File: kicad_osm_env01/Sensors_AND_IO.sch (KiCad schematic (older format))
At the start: 52 parts, among them J4 Conn_01x08, J8 STX-3000, Q5 FK3503010L, Q6 SSM3J328R, U10 ICS-43434, U11 HDC2080, U12 TSL2561, U9 M74VHC1GT14DFT2G

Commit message: updated schematics
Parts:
- removed C44: 100nF, Capacitor_SMD:C_0402_1005Metric, symbol OSM_env01-rescue:C-device-ESP32-EVB_Rev_D-rescue
- removed R102: DNF, Resistor_SMD:R_0603_1608Metric, symbol OSM_env01-rescue:R-device-ESP32-EVB_Rev_D-rescue
- removed R103: 0R, Resistor_SMD:R_0603_1608Metric, symbol OSM_env01-rescue:R-device-ESP32-EVB_Rev_D-rescue
- removed TP49, TP82: Test_Point, TestPoint:TestPoint_THTPad_D1.0mm_Drill0.5mm, symbol OSM_env01-rescue:Test_Point-Connector-ESP32-EVB_Rev_D-rescue
- removed U12: TSL2561, Devtank_PCB_lib:TSL2561T_ALS, symbol OSM_env01-rescue:TSL2561-Devtank-ESP32-EVB_Rev_D-rescue
- added U3: VEML7700-TT, Devtank_PCB_lib:VEML7700-TT, symbol Devtank:VEML7700-TT
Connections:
- wire segments 141 -> 126
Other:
- note removed: "Light Sensor\n"
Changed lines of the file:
@@
 Wire Wire Line
 	3450 1075 3450 1150
-Text Notes 8900 4150 0    118  ~ 0
-Light Sensor\n
 $Sheet
 S 8600 4875 900  1000
@@
 Wire Wire Line
 	10100 5350 10050 5350
-$Comp
-L OSM_env01-rescue:R-device-ESP32-EVB_Rev_D-rescue R?
-U 1 1 6095989E
-P 7975 3125
-AR Path="/6095989E" Ref="R?"  Part="1"
-AR Path="/608F4675/6095989E" Ref="R102"  Part="1"
-F 0 "R102" H 8045 3171 50  0000 L CNN
-F 1 "DNF" H 8045 3080 50  0000 L CNN
-F 2 "Resistor_SMD:R_0603_1608Metric" V 7905 3125 50  0001 C CNN
-F 3 "" H 7975 3125 50  0001 C CNN
-	1    7975 3125
-	1    0    0    -1
-$EndComp
-$Comp
-L OSM_env01-rescue:R-device-ESP32-EVB_Rev_D-rescue R?
-U 1 1 609598A4
-P 7975 3500
-AR Path="/609598A4" Ref="R?"  Part="1"
-AR Path="/608F4675/609598A4" Ref="R103"  Part="1"
-F 0 "R103" H 8045 3546 50  0000 L CNN
-F 1 "0R" H 8045 3455 50  0000 L CNN
-F 2 "Resistor_SMD:R_0603_1608Metric" V 7905 3500 50  0001 C CNN
-F 3 "" H 7975 3500 50  0001 C CNN
-	1    7975 3500
-	1    0    0    -1
-$EndComp
-Wire Wire Line
-	7975 3300 7975 3275
-Wire Wire Line
-	7975 3350 7975 3300
-Connection ~ 7975 3300
-$Comp
-L power:+3V3 #PWR?
-U 1 1 609598AD
-P 8775 2775
-AR Path="/609598AD" Ref="#PWR?"  Part="1"
-AR Path="/608F4675/609598AD" Ref="#PWR089"  Part="1"
-F 0 "#PWR089" H 8775 2625 50  0001 C CNN
-F 1 "+3V3" H 8790 2948 50  0000 C CNN
-F 2 "" H 8775 2775 50  0001 C CNN
-F 3 "" H 8775 2775 50  0001 C CNN
-	1    8775 2775
-	1    0    0    -1
-$EndComp
-$Comp
-L power:+3V3 #PWR?
-U 1 1 609598B3
-P 7975 2950
-AR Path="/609598B3" Ref="#PWR?"  Part="1"
-AR Path="/608F4675/609598B3" Ref="#PWR085"  Part="1"
-F 0 "#PWR085" H 7975 2800 50  0001 C CNN
-F 1 "+3V3" H 7990 3123 50  0000 C CNN
-F 2 "" H 7975 2950 50  0001 C CNN
-F 3 "" H 7975 2950 50  0001 C CNN
-	1    7975 2950
-	1    0    0    -1
-$EndComp
-Wire Wire Line
-	7975 2975 7975 2950
-$Comp
-L OSM_env01-rescue:GND-ESP32-EVB_Rev_D #PWR?
-U 1 1 609598BA
-P 7975 3725
-AR Path="/609598BA" Ref="#PWR?"  Part="1"
-AR Path="/608F4675/609598BA" Ref="#PWR086"  Part="1"
-F 0 "#PWR086" H 7975 3475 50  0001 C CNN
-F 1 "GND" H 7980 3552 50  0000 C CNN
-F 2 "" H 7975 3725 60  0000 C CNN
-F 3 "" H 7975 3725 60  0000 C CNN
-	1    7975 3725
-	1    0    0    -1
-$EndComp
-$Comp
-L OSM_env01-rescue:GND-ESP32-EVB_Rev_D #PWR?
-U 1 1 609598C0
-P 8900 3725
-AR Path="/609598C0" Ref="#PWR?"  Part="1"
-AR Path="/608F4675/609598C0" Ref="#PWR090"  Part="1"
-F 0 "#PWR090" H 8900 3475 50  0001 C CNN
-F 1 "GND" H 8905 3552 50  0000 C CNN
-F 2 "" H 8900 3725 60  0000 C CNN
-F 3 "" H 8900 3725 60  0000 C CNN
-	1    8900 3725
-	1    0    0    -1
-$EndComp
-Wire Wire Line
-	8900 3725 8900 3475
-Wire Wire Line
-	8900 3475 8975 3475
-Wire Wire Line
-	7975 3725 7975 3650
-$Comp
-L OSM_env01-rescue:C-device-ESP32-EVB_Rev_D-rescue C?
-U 1 1 609598CB
-P 8625 2975
-AR Path="/609598CB" Ref="C?"  Part="1"
-AR Path="/608F4675/609598CB" Ref="C44"  Part="1"
-F 0 "C44" H 8750 3075 50  0000 L CNN
-F 1 "100nF" H 8750 3000 50  0000 L CNN
-F 2 "Capacitor_SMD:C_0402_1005Metric" H 8663 2825 50  0001 C CNN
-F 3 "" H 8625 2975 50  0001 C CNN
-	1    8625 2975
-	0    -1   -1   0
-$EndComp
-Wire Wire Line
-	8975 3125 8775 3125
-$Comp
-L OSM_env01-rescue:TSL2561-Devtank-ESP32-EVB_Rev_D-rescue U?
-U 1 1 609598E0
-P 9475 3300
-AR Path="/609598E0" Ref="U?"  Part="1"
-AR Path="/608F4675/609598E0" Ref="U12"  Part="1"
-F 0 "U12" H 9487 3740 50  0000 C CNN
-F 1 "TSL2561" H 9487 3649 50  0000 C CNN
-F 2 "Devtank_PCB_lib:TSL2561T_ALS" H 9500 2950 50  0001 C CNN
-F 3 "http://www.ti.com/lit/ds/symlink/hdc1080.pdf" H 9275 3625 50  0001 C CNN
-	1    9475 3300
-	1    0    0    -1
-$EndComp
-Wire Wire Line
-	10000 3125 10550 3125
-Wire Wire Line
-	10000 3600 10575 3600
-Wire Wire Line
-	8775 2775 8775 2975
-Connection ~ 8775 2975
-Wire Wire Line
-	8775 2975 8775 3125
-$Comp
-L OSM_env01-rescue:GND-ESP32-EVB_Rev_D #PWR?
-U 1 1 609598EB
-P 8375 2975
-AR Path="/609598EB" Ref="#PWR?"  Part="1"
-AR Path="/608F4675/609598EB" Ref="#PWR088"  Part="1"
-F 0 "#PWR088" H 8375 2725 50  0001 C CNN
-F 1 "GND" H 8380 2802 50  0000 C CNN
-F 2 "" H 8375 2975 60  0000 C CNN
-F 3 "" H 8375 2975 60  0000 C CNN
-	1    8375 2975
-	1    0    0    -1
-$EndComp
-Wire Wire Line
-	8375 2975 8475 2975
-Wire Wire Line
-	7975 3300 8975 3300
 Text Notes 8125 6300 0    118  ~ 0
 Sound Level Meter\n
@@
 Text HLabel 7650 1025 0    50   Input ~ 0
 SDA
-Text HLabel 10550 3125 2    50   Input ~ 0
-SDA
-Text HLabel 10575 3600 2    50   Input ~ 0
-SCL
-Wire Wire Line
-	10000 3600 10000 3475
 Wire Wire Line
 	10200 5450 10050 5450
@@
 Text HLabel 8275 5350 0    50   Input ~ 0
 MIC_GND
-Wire Wire Line
-	10000 3300 10400 3300
 Wire Wire Line
 	8250 5475 8375 5475
@@
 $Comp
 L OSM_env01-rescue:Test_Point-Connector-ESP32-EVB_Rev_D-rescue TP?
-U 1 1 60A1D280
-P 10400 3300
-AR Path="/5F6F7717/60A1D280" Ref="TP?"  Part="1"
-AR Path="/60A1D280" Ref="TP?"  Part="1"
-AR Path="/608F4675/60A1D280" Ref="TP82"  Part="1"
-F 0 "TP82" V 10400 3575 50  0000 C CNN
-F 1 "Test_Point" V 10475 3525 50  0001 C CNN
-F 2 "TestPoint:TestPoint_THTPad_D1.0mm_Drill0.5mm" H 10600 3300 50  0001 C CNN
-F 3 "~" H 10600 3300 50  0001 C CNN
-	1    10400 3300
-	0    1    1    0
-$EndComp
-$Comp
-L OSM_env01-rescue:Test_Point-Connector-ESP32-EVB_Rev_D-rescue TP?
-U 1 1 60A24650
-P 7975 3300
-AR Path="/5F6F7717/60A24650" Ref="TP?"  Part="1"
-AR Path="/60A24650" Ref="TP?"  Part="1"
-AR Path="/608F4675/60A24650" Ref="TP49"  Part="1"
-F 0 "TP49" V 7975 3575 50  0000 C CNN
-F 1 "Test_Point" V 8050 3525 50  0001 C CNN
-F 2 "TestPoint:TestPoint_THTPad_D1.0mm_Drill0.5mm" H 8175 3300 50  0001 C CNN
-F 3 "~" H 8175 3300 50  0001 C CNN
-	1    7975 3300
-	0    -1   1    0
-$EndComp
-$Comp
-L OSM_env01-rescue:Test_Point-Connector-ESP32-EVB_Rev_D-rescue TP?
 U 1 1 60A2CE09
 P 8250 5475
@@
 	1    0    0    -1
 $EndComp
+$Comp
+L Devtank:VEML7700-TT U3
+U 1 1 617460B6
+P 8600 3225
+F 0 "U3" H 9400 3612 60  0000 C CNN
+F 1 "VEML7700-TT" H 9400 3506 60  0000 C CNN
+F 2 "Devtank_PCB_lib:VEML7700-TT" H 9400 3465 60  0001 C CNN
+F 3 "" H 8600 3225 60  0000 C CNN
+	1    8600 3225
+	1    0    0    -1
+$EndComp

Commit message: schematics awaiting review
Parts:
- removed U11: HDC2080, Devtank_PCB_lib:HDC2080, symbol OSM_env01-rescue:HDC2080-Devtank-ESP32-EVB_Rev_D-rescue
- added C55: DNF, symbol device:C
- added C56: 100nF, symbol device:C
- added R29: 0R, symbol device:R
- added TP13, TP14, TP49, TP56: Test_Point, TestPoint:TestPoint_THTPad_D1.0mm_Drill0.5mm, symbol OSM_env01-rescue:Test_Point-Connector-ESP32-EVB_Rev_D-rescue
- added U11: HDC2080, symbol Devtank:HDC2080
- R97: value DNF -> 100k
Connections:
- net labels removed: CT-, LR, MIC_LR, WS
- wire segments 126 -> 148
- no-connect marks 4 -> 6
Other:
- note added: "Light Sensor\n\n"
- note added: "Note: Can use HDC1080/2080. For HTU21D leave pad 3,4 and ep unconnected"
- note added: "Pulse Inputs\n"
- note removed: "Pulse 2\n\n"
- note removed: "Water Pump\n"
- moved on the sheet: C39, C40, C41, C42, C43, C45, C71, C73, D11, J4, J8, Q5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

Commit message: rough layout with throwdown of parts
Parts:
- removed TP52, TP53: Test_Point, TestPoint:TestPoint_THTPad_D1.0mm_Drill0.5mm, symbol OSM_env01-rescue:Test_Point-Connector-ESP32-EVB_Rev_D-rescue
- C42: footprint Capacitor_SMD:C_0603_1608Metric -> Capacitor_SMD:C_0402_1005Metric
- C55: footprint (none) -> Capacitor_SMD:C_0603_1608Metric
- C56: footprint (none) -> Capacitor_SMD:C_0402_1005Metric
- R100: value 0R -> DNF
- R29: footprint (none) -> Resistor_SMD:R_0603_1608Metric
- R88: footprint Resistor_SMD:R_0805_2012Metric -> Resistor_SMD:R_1206_3216Metric
- TP13, TP14, TP42, TP43, TP44, TP45, TP46, TP47, TP48, TP49, TP50, TP51, TP56, TP68, TP88: footprint TestPoint:TestPoint_THTPad_D1.0mm_Drill0.5mm -> TestPoint:TestPoint_Pad_D1.5mm
- U10: footprint Devtank_PCB_lib:MIC_ICS-43434 -> Devtank_PCB_lib:ICS-43434
- U11: footprint (none) -> Devtank_PCB_lib:HDC2080D
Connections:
- net labels removed: +3V3_A, AUDIO_OP, GNDA, MIC_GND
- wire segments 148 -> 140
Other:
- note removed: "Sound Level Meter\n"

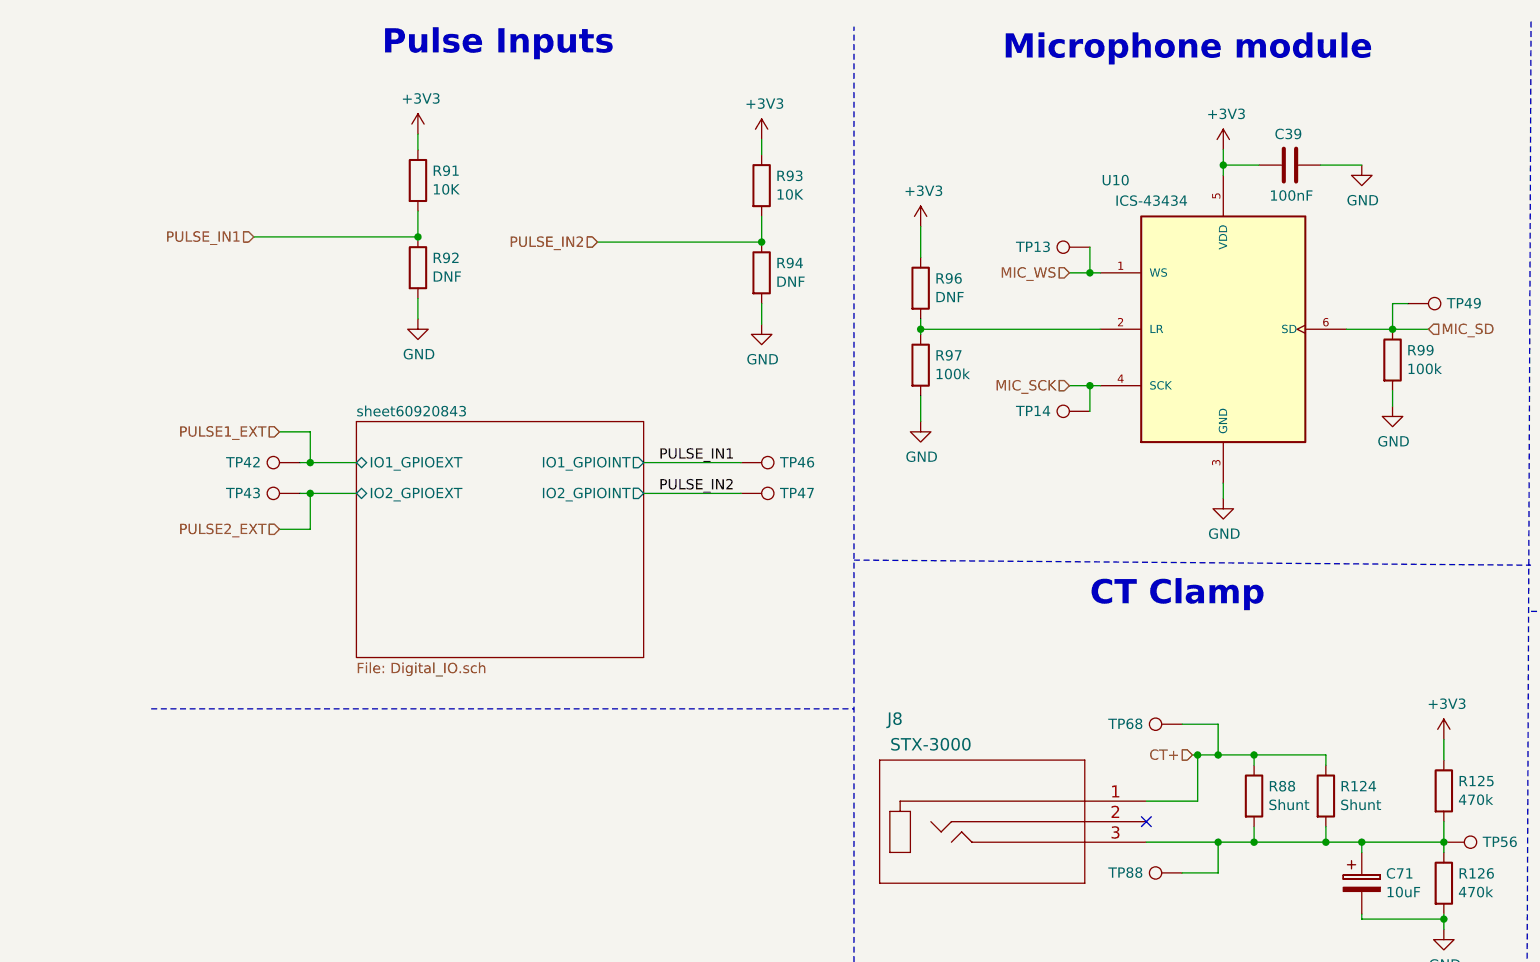
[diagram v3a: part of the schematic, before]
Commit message: updated schematics
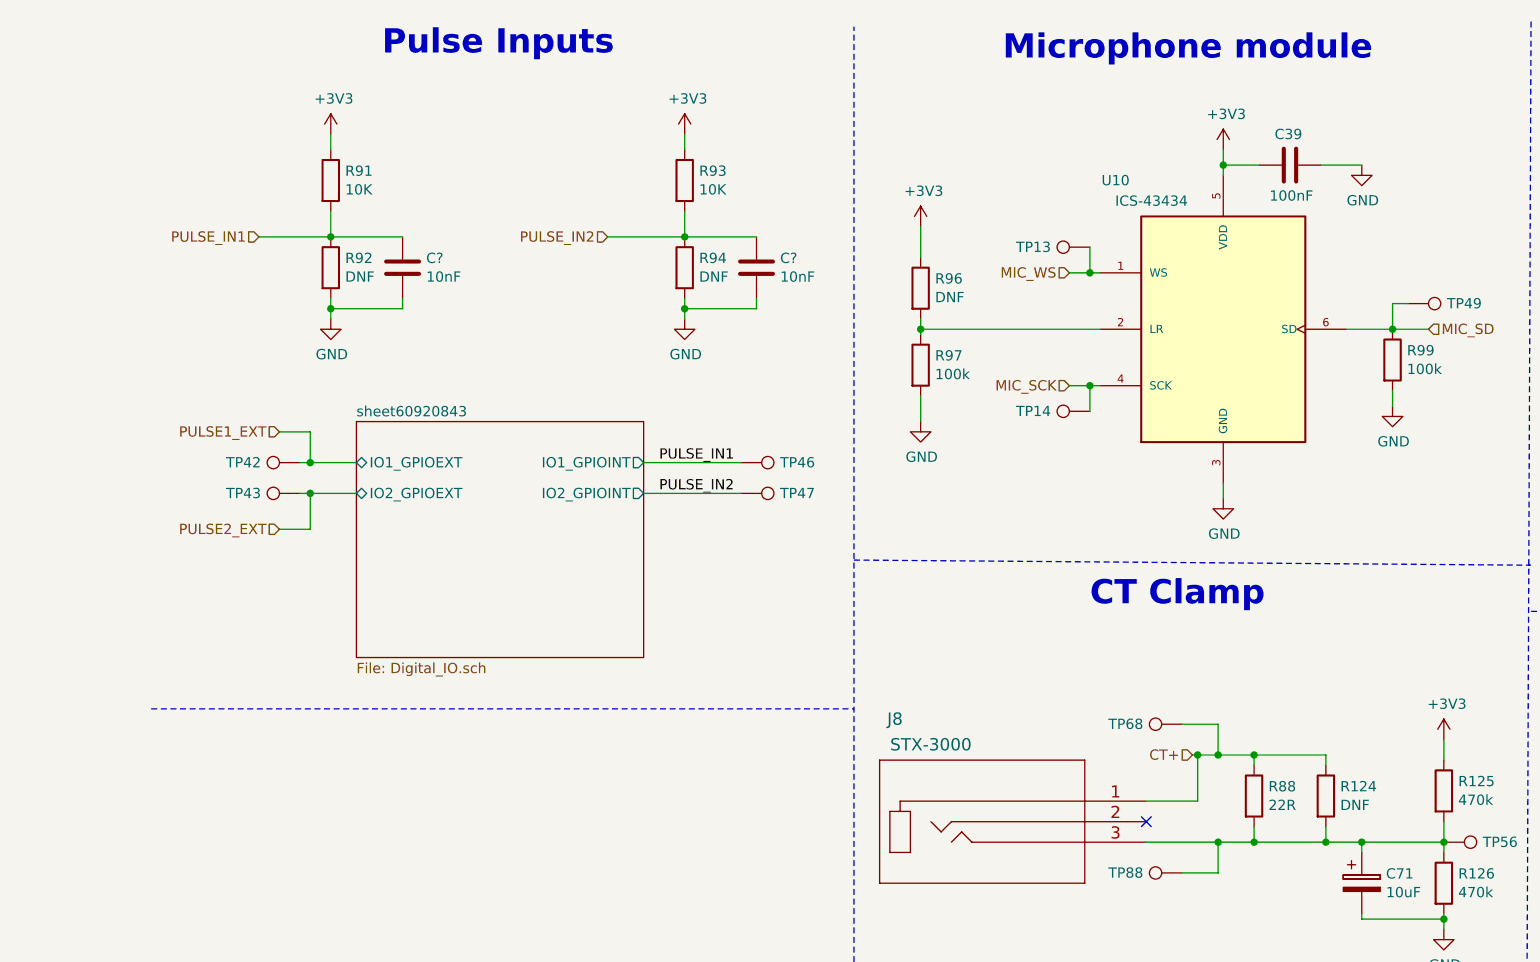
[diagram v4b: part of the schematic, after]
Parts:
- added C? (x2): 10nF, symbol device:C
- C40: footprint Capacitor_SMD:C_0805_2012Metric -> Capacitor_SMD:C_0603_1608Metric
- R124: value Shunt -> DNF
- R88: value Shunt -> 22R
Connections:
- net GND: now also C?.2, C?.2
- net PULSE_IN1: now also C?.1
- net PULSE_IN2: now also C?.1
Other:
- moved on the sheet: R91, R92, R93, R94
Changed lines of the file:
@@
 L OSM_env01-rescue:R-device-ESP32-EVB_Rev_D-rescue R?
 U 1 1 6092084A
-P 1775 1275
+P 1350 1275
 AR Path="/6092084A" Ref="R?"  Part="1"
 AR Path="/608F4675/6092084A" Ref="R91"  Part="1"
-F 0 "R91" H 1845 1321 50  0000 L CNN
-F 1 "10K" H 1845 1230 50  0000 L CNN
-F 2 "Resistor_SMD:R_0603_1608Metric" V 1705 1275 50  0001 C CNN
-F 3 "" H 1775 1275 50  0001 C CNN
-	1    1775 1275
+F 0 "R91" H 1420 1321 50  0000 L CNN
+F 1 "10K" H 1420 1230 50  0000 L CNN
+F 2 "Resistor_SMD:R_0603_1608Metric" V 1280 1275 50  0001 C CNN
+F 3 "" H 1350 1275 50  0001 C CNN
+	1    1350 1275
 	1    0    0    -1
 $EndComp
@@
 L power:+3V3 #PWR?
 U 1 1 60920850
-P 1775 1050
+P 1350 1050
 AR Path="/60920850" Ref="#PWR?"  Part="1"
 AR Path="/608F4675/60920850" Ref="#PWR068"  Part="1"
-F 0 "#PWR068" H 1775 900 50  0001 C CNN
-F 1 "+3V3" H 1790 1223 50  0000 C CNN
-F 2 "" H 1775 1050 50  0001 C CNN
-F 3 "" H 1775 1050 50  0001 C CNN
-	1    1775 1050
-	1    0    0    -1
-$EndComp
-Wire Wire Line
-	1775 1550 1775 1425
+F 0 "#PWR068" H 1350 900 50  0001 C CNN
+F 1 "+3V3" H 1365 1223 50  0000 C CNN
+F 2 "" H 1350 1050 50  0001 C CNN
+F 3 "" H 1350 1050 50  0001 C CNN
+	1    1350 1050
+	1    0    0    -1
+$EndComp
+Wire Wire Line
+	1350 1550 1350 1425
 $Sheet
 S 1475 2450 1400 1150
@@
 	1200 2800 1250 2800
 Wire Wire Line
-	975  1550 1775 1550
+	1000 1550 1350 1550
 $Comp
 L OSM_env01-rescue:R-device-ESP32-EVB_Rev_D-rescue R?
 U 1 1 6092087F
-P 1775 1700
+P 1350 1700
 AR Path="/6092087F" Ref="R?"  Part="1"
 AR Path="/608F4675/6092087F" Ref="R92"  Part="1"
-F 0 "R92" H 1845 1746 50  0000 L CNN
-F 1 "DNF" H 1845 1655 50  0000 L CNN
-F 2 "Resistor_SMD:R_0603_1608Metric" V 1705 1700 50  0001 C CNN
-F 3 "" H 1775 1700 50  0001 C CNN
-	1    1775 1700
-	1    0    0    -1
-$EndComp
-Connection ~ 1775 1550
+F 0 "R92" H 1420 1746 50  0000 L CNN
+F 1 "DNF" H 1420 1655 50  0000 L CNN
+F 2 "Resistor_SMD:R_0603_1608Metric" V 1280 1700 50  0001 C CNN
+F 3 "" H 1350 1700 50  0001 C CNN
+	1    1350 1700
+	1    0    0    -1
+$EndComp
+Connection ~ 1350 1550
 $Comp
 L OSM_env01-rescue:GND-ESP32-EVB_Rev_D #PWR?
 U 1 1 60920886
-P 1775 1950
+P 1350 1950
 AR Path="/60920886" Ref="#PWR?"  Part="1"
 AR Path="/608F4675/60920886" Ref="#PWR069"  Part="1"
-F 0 "#PWR069" H 1775 1700 50  0001 C CNN
-F 1 "GND" H 1780 1777 50  0000 C CNN
-F 2 "" H 1775 1950 60  0000 C CNN
-F 3 "" H 1775 1950 60  0000 C CNN
-	1    1775 1950
-	1    0    0    -1
-$EndComp
-Wire Wire Line
-	1775 1950 1775 1850
+F 0 "#PWR069" H 1350 1700 50  0001 C CNN
+F 1 "GND" H 1355 1777 50  0000 C CNN
+F 2 "" H 1350 1950 60  0000 C CNN
+F 3 "" H 1350 1950 60  0000 C CNN
+	1    1350 1950
+	1    0    0    -1
+$EndComp
+Wire Wire Line
+	1350 1950 1350 1900
 $Comp
 L OSM_env01-rescue:R-device-ESP32-EVB_Rev_D-rescue R?
 U 1 1 6092088E
-P 3450 1300
+P 3075 1275
 AR Path="/6092088E" Ref="R?"  Part="1"
 AR Path="/608F4675/6092088E" Ref="R93"  Part="1"
-F 0 "R93" H 3520 1346 50  0000 L CNN
-F 1 "10K" H 3520 1255 50  0000 L CNN
-F 2 "Resistor_SMD:R_0603_1608Metric" V 3380 1300 50  0001 C CNN
-F 3 "" H 3450 1300 50  0001 C CNN
-	1    3450 1300
+F 0 "R93" H 3145 1321 50  0000 L CNN
+F 1 "10K" H 3145 1230 50  0000 L CNN
+F 2 "Resistor_SMD:R_0603_1608Metric" V 3005 1275 50  0001 C CNN
+F 3 "" H 3075 1275 50  0001 C CNN
+	1    3075 1275
 	1    0    0    -1
 $EndComp
@@
 L power:+3V3 #PWR?
 U 1 1 60920894
-P 3450 1075
+P 3075 1050
 AR Path="/60920894" Ref="#PWR?"  Part="1"
 AR Path="/608F4675/60920894" Ref="#PWR071"  Part="1"
-F 0 "#PWR071" H 3450 925 50  0001 C CNN
-F 1 "+3V3" H 3465 1248 50  0000 C CNN
-F 2 "" H 3450 1075 50  0001 C CNN
-F 3 "" H 3450 1075 50  0001 C CNN
-	1    3450 1075
-	1    0    0    -1
-$EndComp
-Wire Wire Line
-	3450 1575 3450 1450
-Wire Wire Line
-	2650 1575 3450 1575
+F 0 "#PWR071" H 3075 900 50  0001 C CNN
+F 1 "+3V3" H 3090 1223 50  0000 C CNN
+F 2 "" H 3075 1050 50  0001 C CNN
+F 3 "" H 3075 1050 50  0001 C CNN
+	1    3075 1050
+	1    0    0    -1
+$EndComp
+Wire Wire Line
+	3075 1550 3075 1425
+Wire Wire Line
+	2700 1550 3075 1550
 $Comp
 L OSM_env01-rescue:R-device-ESP32-EVB_Rev_D-rescue R?
 U 1 1 6092089D
-P 3450 1725
+P 3075 1700
 AR Path="/6092089D" Ref="R?"  Part="1"
 AR Path="/608F4675/6092089D" Ref="R94"  Part="1"
-F 0 "R94" H 3520 1771 50  0000 L CNN
-F 1 "DNF" H 3520 1680 50  0000 L CNN
-F 2 "Resistor_SMD:R_0603_1608Metric" V 3380 1725 50  0001 C CNN
-F 3 "" H 3450 1725 50  0001 C CNN
-	1    3450 1725
-	1    0    0    -1
-$EndComp
-Connection ~ 3450 1575
+F 0 "R94" H 3145 1746 50  0000 L CNN
+F 1 "DNF" H 3145 1655 50  0000 L CNN
+F 2 "Resistor_SMD:R_0603_1608Metric" V 3005 1700 50  0001 C CNN
+F 3 "" H 3075 1700 50  0001 C CNN
+	1    3075 1700
+	1    0    0    -1
+$EndComp
+Connection ~ 3075 1550
 $Comp
 L OSM_env01-rescue:GND-ESP32-EVB_Rev_D #PWR?
 U 1 1 609208A4
-P 3450 1975
+P 3075 1950
 AR Path="/609208A4" Ref="#PWR?"  Part="1"
 AR Path="/608F4675/609208A4" Ref="#PWR072"  Part="1"
-F 0 "#PWR072" H 3450 1725 50  0001 C CNN
-F 1 "GND" H 3455 1802 50  0000 C CNN
-F 2 "" H 3450 1975 60  0000 C CNN
-F 3 "" H 3450 1975 60  0000 C CNN
-	1    3450 1975
-	1    0    0    -1
-$EndComp
-Wire Wire Line
-	3450 1975 3450 1875
-Wire Wire Line
-	1775 1050 1775 1125
-Wire Wire Line
-	3450 1075 3450 1150
+F 0 "#PWR072" H 3075 1700 50  0001 C CNN
+F 1 "GND" H 3080 1777 50  0000 C CNN
+F 2 "" H 3075 1950 60  0000 C CNN
+F 3 "" H 3075 1950 60  0000 C CNN
+	1    3075 1950
+	1    0    0    -1
+$EndComp
+Wire Wire Line
+	3075 1950 3075 1900
+Wire Wire Line
+	1350 1050 1350 1125
+Wire Wire Line
+	3075 1050 3075 1125
 $Comp
 L OSM_env01-rescue:C-device-ESP32-EVB_Rev_D-rescue C?
@@
 F 0 "C40" H 1325 6450 50  0000 L CNN
 F 1 "10uF" H 1325 6350 50  0000 L CNN
-F 2 "Capacitor_SMD:C_0805_2012Metric" H 1263 6250 50  0001 C CNN
+F 2 "Capacitor_SMD:C_0603_1608Metric" H 1263 6250 50  0001 C CNN
 F 3 "" H 1225 6400 50  0001 C CNN
 	1    1225 6400
@@
 AR Path="/608F4675/611CCBED" Ref="R124"  Part="1"
 F 0 "R124" H 6270 4321 50  0000 L CNN
-F 1 "Shunt" H 6270 4230 50  0000 L CNN
+F 1 "DNF" H 6270 4230 50  0000 L CNN
 F 2 "Resistor_SMD:R_1206_3216Metric" V 6130 4275 50  0001 C CNN
 F 3 "" H 6200 4275 50  0001 C CNN
@@
 AR Path="/608F4675/6073EBF7" Ref="R88"  Part="1"
 F 0 "R88" H 5920 4321 50  0000 L CNN
-F 1 "Shunt" H 5920 4230 50  0000 L CNN
+F 1 "22R" H 5920 4230 50  0000 L CNN
 F 2 "Resistor_SMD:R_1206_3216Metric" V 5780 4275 50  0001 C CNN
 F 3 "" H 5850 4275 50  0001 C CNN
@@
 	1    0    0    -1
 $EndComp
-Text HLabel 975  1550 0    50   Input ~ 0
+Text HLabel 1000 1550 0    50   Input ~ 0
 PULSE_IN1
-Text HLabel 2650 1575 0    50   Input ~ 0
+Text HLabel 2700 1550 0    50   Input ~ 0
 PULSE_IN2
 Wire Wire Line
@@
 	1    0    0    -1
 $EndComp
+$Comp
+L device:C C?
+U 1 1 619BA90A
+P 1700 1700
+F 0 "C?" H 1815 1746 50  0000 L CNN
+F 1 "10nF" H 1815 1655 50  0000 L CNN
+F 2 "" H 1738 1550 50  0001 C CNN
+F 3 "" H 1700 1700 50  0001 C CNN
+	1    1700 1700
+	1    0    0    -1
+$EndComp
+Wire Wire Line
+	1350 1900 1700 1900
+Wire Wire Line
+	1700 1900 1700 1850
+Connection ~ 1350 1900
+Wire Wire Line
+	1350 1900 1350 1850
+Wire Wire Line
+	1350 1550 1700 1550
+$Comp
+L device:C C?
+U 1 1 619EFDCD
+P 3425 1700
+F 0 "C?" H 3540 1746 50  0000 L CNN
+F 1 "10nF" H 3540 1655 50  0000 L CNN
+F 2 "" H 3463 1550 50  0001 C CNN
+F 3 "" H 3425 1700 50  0001 C CNN
+	1    3425 1700
+	1    0    0    -1
+$EndComp
+Wire Wire Line
+	3075 1900 3425 1900
+Wire Wire Line
+	3425 1900 3425 1850
+Wire Wire Line
+	3075 1550 3425 1550
+Connection ~ 3075 1900
+Wire Wire Line
+	3075 1900 3075 1850
 $EndSCHEMATC
